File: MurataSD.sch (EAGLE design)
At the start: 2 parts, among them U1 IC_BLE_LBCA2HNZYZ-711, U100 BOARD_MMC

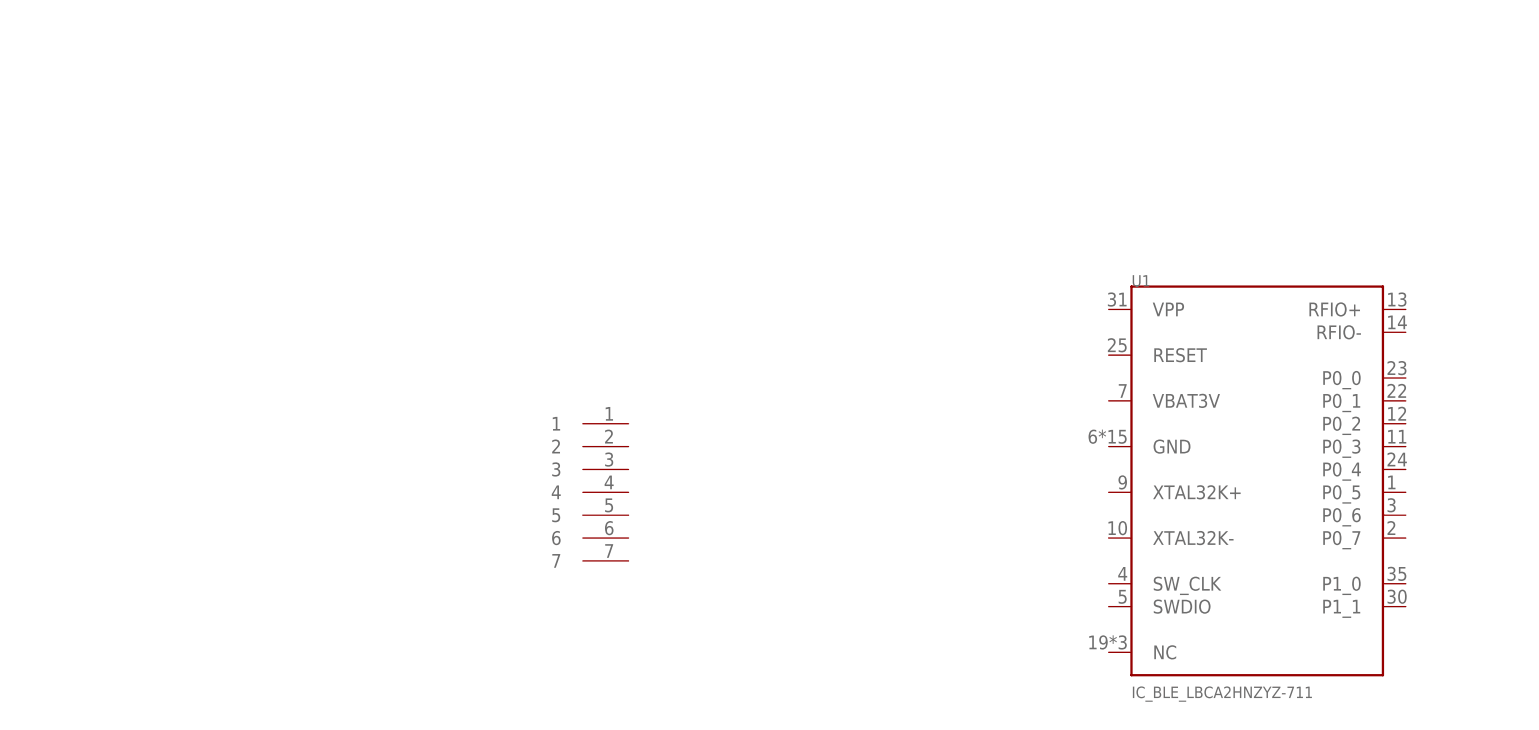
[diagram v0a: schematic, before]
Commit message: schematic update
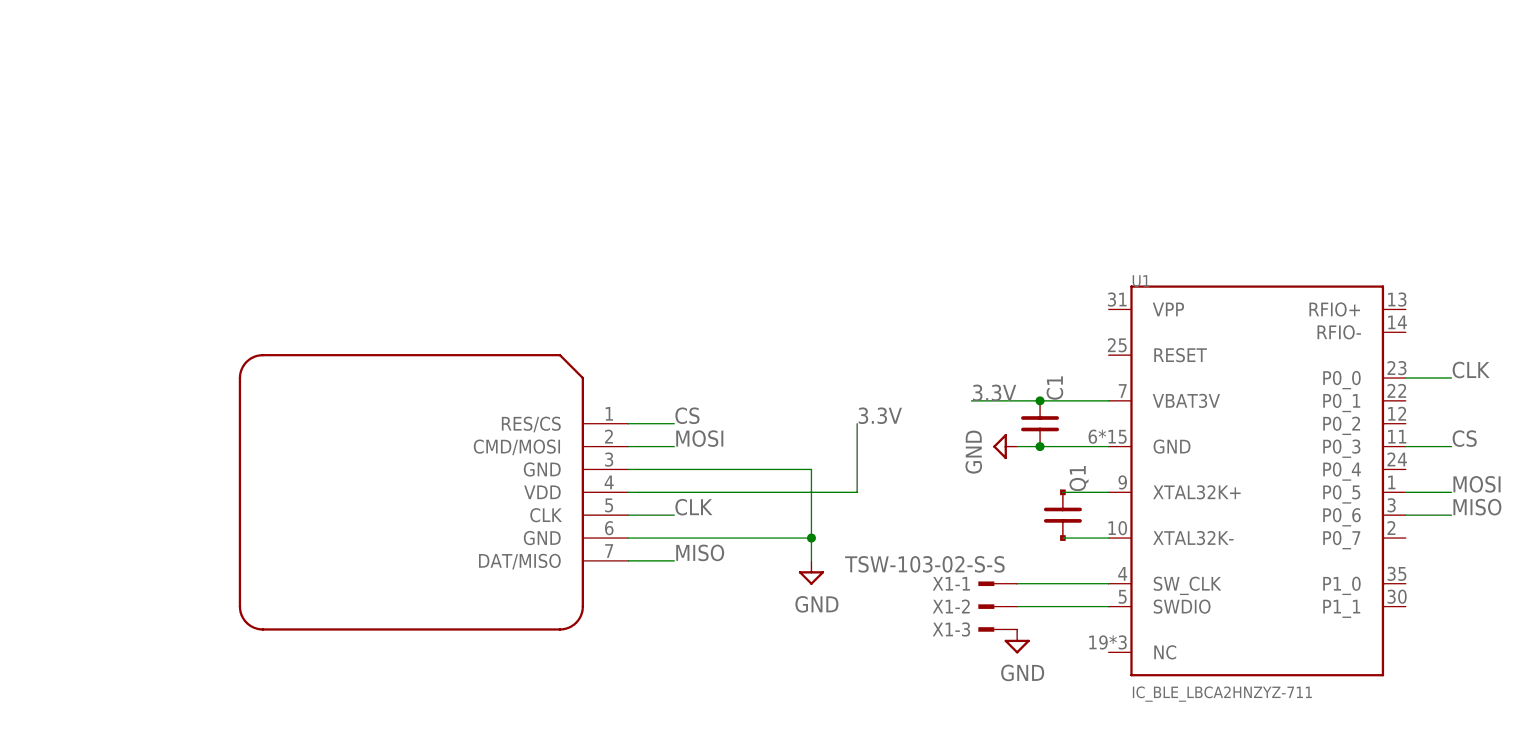
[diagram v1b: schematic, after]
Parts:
- added C1: (no value), mylib:C_PAD_PAD_1005
- added Q1: (no value), mylib:C_PAD_PAD_3216
- added X1: TSW-103-02-S-S, con-samtec.local:TSW-103-02-S-S
- renumbered U100 to U2
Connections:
- new net 3.3V: C1.1, U1.VBAT3V, U2.VDD
- new net CLK: U1.P0_0, U2.CLK
- new net CS: U1.P0_3, U2.RES/CS
- new net GND: C1.2, U1.GND, U2.GND@1, U2.GND@2, X1-3.1
- new net MISO: U1.P0_6, U2.DAT/MISO
- new net MOSI: U1.P0_5, U2.CMD/MOSI
- new net N$1: Q1.1, U1.XTAL32K+
- new net N$2: Q1.2, U1.XTAL32K-
- new net N$3: U1.SW_CLK, X1-1.1
- new net N$4: U1.SWDIO, X1-2.1
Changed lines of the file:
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@@
 <parts>
 <part name="FRAME1" library="frames" deviceset="A4L-LOC" device=""/>
-<part name="U100" library="mylib" deviceset="BOARD_MMC" device=""/>
+<part name="U2" library="mylib" deviceset="BOARD_MMC" device=""/>
 <part name="U1" library="mylib" deviceset="IC_BLE_LBCA2HNZYZ-711" device=""/>
+<part name="SUPPLY1" library="mylib" deviceset="GND" device=""/>
+<part name="SUPPLY2" library="mylib" deviceset="GND" device=""/>
+<part name="C1" library="mylib" deviceset="C_PAD_PAD_" device="1005"/>
+<part name="Q1" library="mylib" deviceset="C_PAD_PAD_" device="3216"/>
+<part name="X1" library="con-samtec.local" deviceset="TSW-103-02-S-S" device=""/>
+<part name="SUPPLY3" library="mylib" deviceset="GND" device=""/>
 </parts>
 <sheets>
@@
 <instances>
 <instance part="FRAME1" gate="G$1" x="0" y="0"/>
-<instance part="U100" gate="G$1" x="78.74" y="96.52"/>
+<instance part="U2" gate="G$1" x="78.74" y="96.52"/>
 <instance part="U1" gate="G$1" x="154.94" y="99.06"/>
+<instance part="SUPPLY1" gate="GND" x="124.46" y="101.6" rot="R270"/>
+<instance part="SUPPLY2" gate="GND" x="104.14" y="86.36"/>
+<instance part="C1" gate="G$1" x="129.54" y="104.14"/>
+<instance part="Q1" gate="G$1" x="132.08" y="93.98"/>
+<instance part="X1" gate="-1" x="124.46" y="86.36" rot="MR0"/>
+<instance part="X1" gate="-2" x="124.46" y="83.82" rot="MR0"/>
+<instance part="X1" gate="-3" x="124.46" y="81.28" rot="R180"/>
+<instance part="SUPPLY3" gate="GND" x="127" y="78.74"/>
 </instances>
 <busses>
 </busses>
 <nets>
+<net name="GND" class="0">
+<segment>
+<pinref part="U2" gate="G$1" pin="GND@1"/>
+<pinref part="SUPPLY2" gate="GND" pin="GND"/>
+<wire x1="83.82" y1="99.06" x2="104.14" y2="99.06" width="0.1524" layer="91"/>
+<wire x1="104.14" y1="99.06" x2="104.14" y2="91.44" width="0.1524" layer="91"/>
+<pinref part="U2" gate="G$1" pin="GND@2"/>
+<wire x1="104.14" y1="91.44" x2="104.14" y2="88.9" width="0.1524" layer="91"/>
+<wire x1="83.82" y1="91.44" x2="104.14" y2="91.44" width="0.1524" layer="91"/>
+<junction x="104.14" y="91.44"/>
+</segment>
+<segment>
+<pinref part="SUPPLY1" gate="GND" pin="GND"/>
+<pinref part="C1" gate="G$1" pin="2"/>
+<wire x1="127" y1="101.6" x2="129.54" y2="101.6" width="0.1524" layer="91"/>
+<pinref part="U1" gate="G$1" pin="GND"/>
+<wire x1="129.54" y1="101.6" x2="137.16" y2="101.6" width="0.1524" layer="91"/>
+<junction x="129.54" y="101.6"/>
+</segment>
+<segment>
+<pinref part="X1" gate="-3" pin="1"/>
+<pinref part="SUPPLY3" gate="GND" pin="GND"/>
+</segment>
+</net>
+<net name="3.3V" class="0">
+<segment>
+<pinref part="U2" gate="G$1" pin="VDD"/>
+<wire x1="83.82" y1="96.52" x2="109.22" y2="96.52" width="0.1524" layer="91"/>
+<wire x1="109.22" y1="96.52" x2="109.22" y2="104.14" width="0.1524" layer="91"/>
+<label x="109.22" y="104.14" size="1.778" layer="95"/>
+</segment>
+<segment>
+<pinref part="U1" gate="G$1" pin="VBAT3V"/>
+<pinref part="C1" gate="G$1" pin="1"/>
+<wire x1="137.16" y1="106.68" x2="129.54" y2="106.68" width="0.1524" layer="91"/>
+<wire x1="129.54" y1="106.68" x2="121.92" y2="106.68" width="0.1524" layer="91"/>
+<junction x="129.54" y="106.68"/>
+<label x="121.92" y="106.68" size="1.778" layer="95"/>
+</segment>
+</net>
+<net name="N$1" class="0">
+<segment>
+<pinref part="U1" gate="G$1" pin="XTAL32K+"/>
+<pinref part="Q1" gate="G$1" pin="1"/>
+<wire x1="137.16" y1="96.52" x2="132.08" y2="96.52" width="0.1524" layer="91"/>
+</segment>
+</net>
+<net name="N$2" class="0">
+<segment>
+<pinref part="U1" gate="G$1" pin="XTAL32K-"/>
+<pinref part="Q1" gate="G$1" pin="2"/>
+<wire x1="137.16" y1="91.44" x2="132.08" y2="91.44" width="0.1524" layer="91"/>
+</segment>
+</net>
+<net name="CLK" class="0">
+<segment>
+<pinref part="U2" gate="G$1" pin="CLK"/>
+<wire x1="83.82" y1="93.98" x2="88.9" y2="93.98" width="0.1524" layer="91"/>
+<label x="88.9" y="93.98" size="1.778" layer="95"/>
+</segment>
+<segment>
+<wire x1="170.18" y1="109.22" x2="175.26" y2="109.22" width="0.1524" layer="91"/>
+<pinref part="U1" gate="G$1" pin="P0_0"/>
+<label x="175.26" y="109.22" size="1.778" layer="95"/>
+</segment>
+</net>
+<net name="MOSI" class="0">
+<segment>
+<pinref part="U2" gate="G$1" pin="CMD/MOSI"/>
+<wire x1="83.82" y1="101.6" x2="88.9" y2="101.6" width="0.1524" layer="91"/>
+<label x="88.9" y="101.6" size="1.778" layer="95"/>
+</segment>
+<segment>
+<wire x1="170.18" y1="96.52" x2="175.26" y2="96.52" width="0.1524" layer="91"/>
+<pinref part="U1" gate="G$1" pin="P0_5"/>
+<label x="175.26" y="96.52" size="1.778" layer="95"/>
+</segment>
+</net>
+<net name="CS" class="0">
+<segment>
+<pinref part="U2" gate="G$1" pin="RES/CS"/>
+<wire x1="83.82" y1="104.14" x2="88.9" y2="104.14" width="0.1524" layer="91"/>
+<label x="88.9" y="104.14" size="1.778" layer="95"/>
+</segment>
+<segment>
+<wire x1="170.18" y1="101.6" x2="175.26" y2="101.6" width="0.1524" layer="91"/>
+<pinref part="U1" gate="G$1" pin="P0_3"/>
+<label x="175.26" y="101.6" size="1.778" layer="95"/>
+</segment>
+</net>
+<net name="MISO" class="0">
+<segment>
+<pinref part="U2" gate="G$1" pin="DAT/MISO"/>
+<wire x1="83.82" y1="88.9" x2="88.9" y2="88.9" width="0.1524" layer="91"/>
+<label x="88.9" y="88.9" size="1.778" layer="95"/>
+</segment>
+<segment>
+<wire x1="170.18" y1="93.98" x2="175.26" y2="93.98" width="0.1524" layer="91"/>
+<label x="175.26" y="93.98" size="1.778" layer="95"/>
+<pinref part="U1" gate="G$1" pin="P0_6"/>
+</segment>
+</net>
+<net name="N$3" class="0">
+<segment>
+<pinref part="U1" gate="G$1" pin="SW_CLK"/>
+<wire x1="127" y1="86.36" x2="137.16" y2="86.36" width="0.1524" layer="91"/>
+<pinref part="X1" gate="-1" pin="1"/>
+</segment>
+</net>
+<net name="N$4" class="0">
+<segment>
+<pinref part="U1" gate="G$1" pin="SWDIO"/>
+<wire x1="137.16" y1="83.82" x2="127" y2="83.82" width="0.1524" layer="91"/>
+<pinref part="X1" gate="-2" pin="1"/>
+</segment>
+</net>
 </nets>
 </sheet>

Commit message: [ SD ] update library
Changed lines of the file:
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@@
 <layers>
 <layer number="1" name="Top" color="4" fill="1" visible="no" active="no"/>
+<layer number="2" name="Route2" color="1" fill="3" visible="no" active="no"/>
+<layer number="3" name="Route3" color="4" fill="3" visible="no" active="no"/>
+<layer number="14" name="Route14" color="1" fill="6" visible="no" active="no"/>
+<layer number="15" name="Route15" color="4" fill="6" visible="no" active="no"/>
 <layer number="16" name="Bottom" color="1" fill="1" visible="no" active="no"/>
 <layer number="17" name="Pads" color="2" fill="1" visible="no" active="no"/>
@@
 <layer number="132" name="bAdjust" color="7" fill="1" visible="no" active="yes"/>
 <layer number="144" name="Drill_legend" color="7" fill="1" visible="yes" active="yes"/>
+<layer number="145" name="DrillLegend_01-16" color="2" fill="9" visible="no" active="yes"/>
+<layer number="146" name="DrillLegend_01-20" color="3" fill="9" visible="no" active="yes"/>
 <layer number="151" name="HeatSink" color="7" fill="1" visible="yes" active="yes"/>
 <layer number="152" name="_bDocu" color="7" fill="1" visible="yes" active="yes"/>

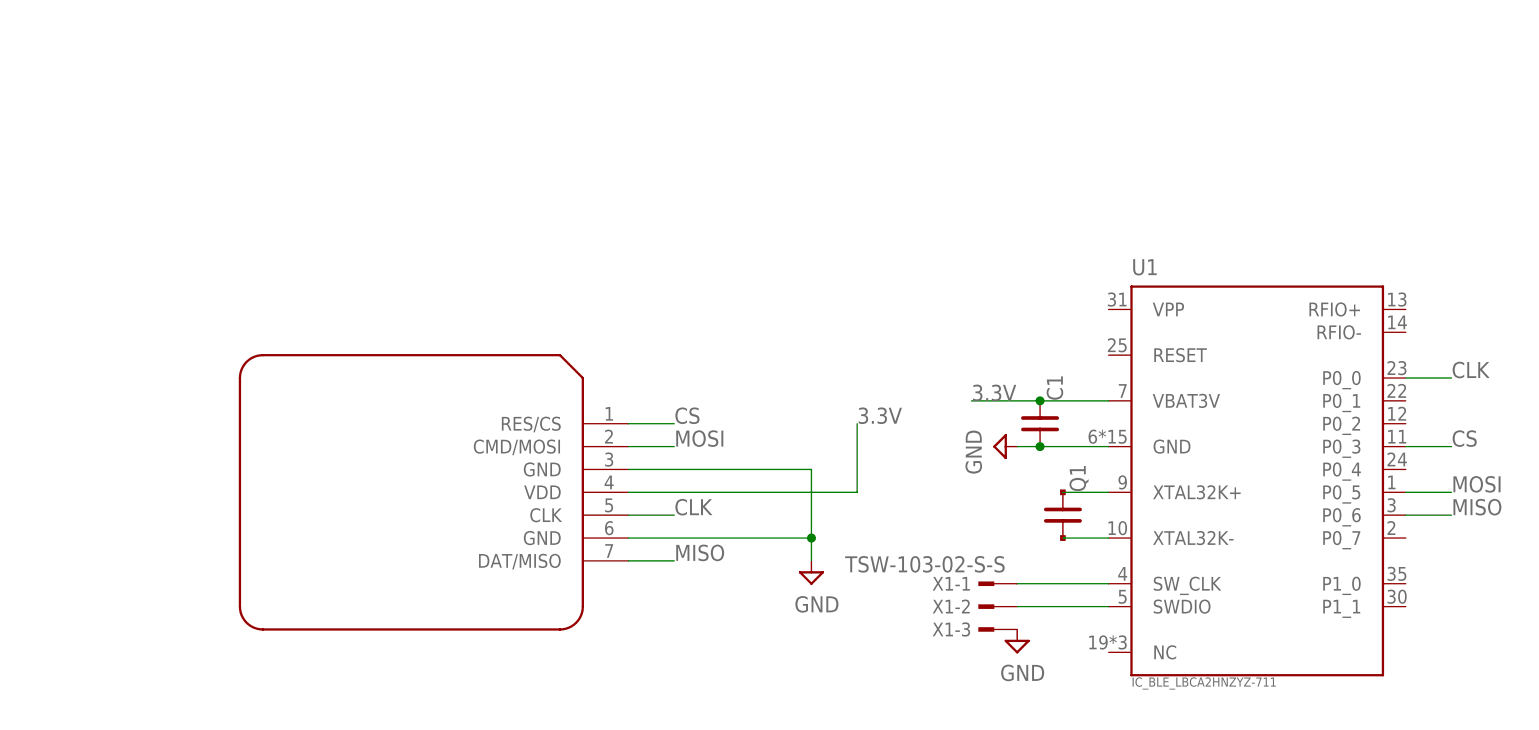
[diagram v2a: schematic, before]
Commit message: [ SD ] library update; add SWD connector; add Flash;
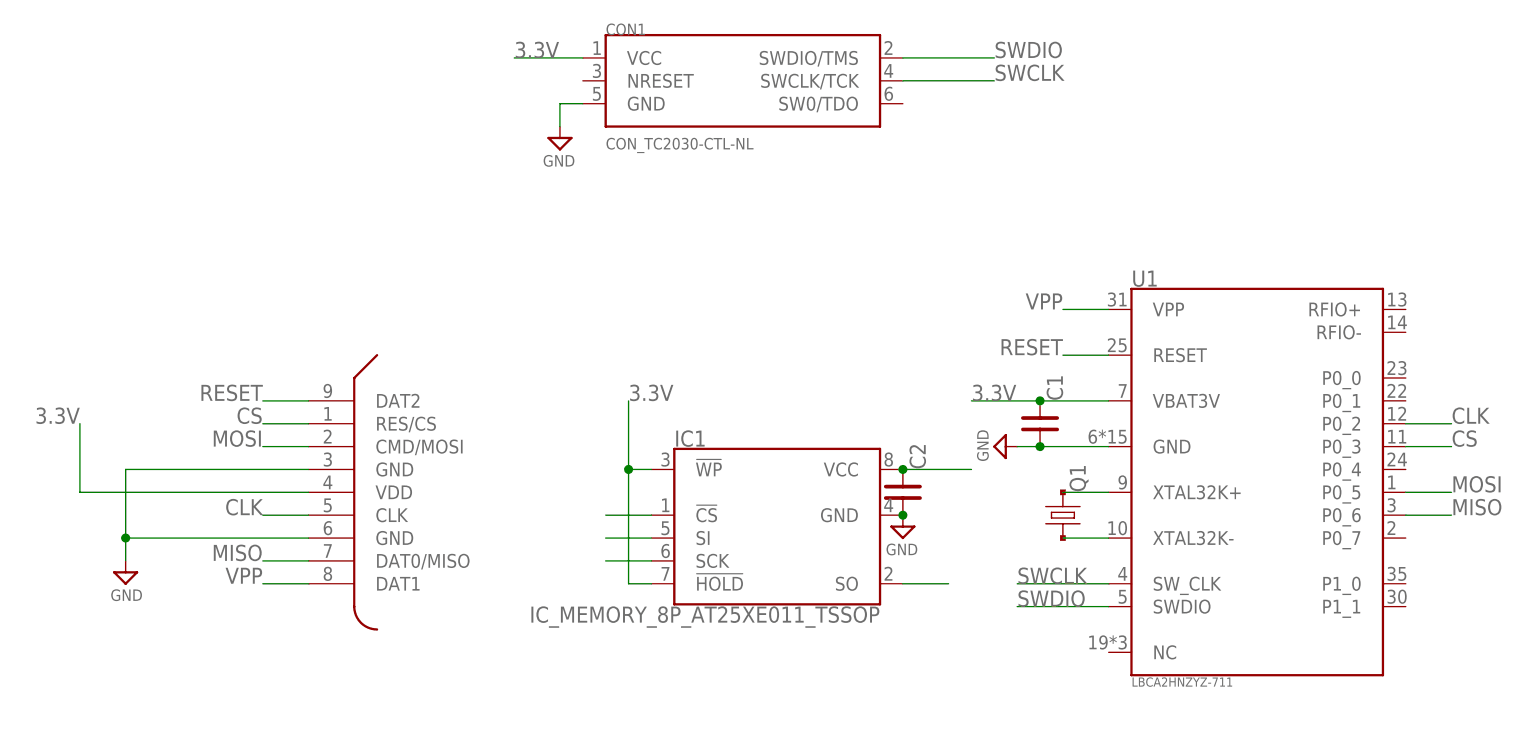
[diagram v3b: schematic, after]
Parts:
- removed X1: TSW-103-02-S-S, con-samtec.local:TSW-103-02-S-S
- added C2: (no value), mylib:C_SMD_0.1U_1005
- added CON1: CON_TC2030-CTL-NL, mylib:CON_TC2030-CTL-NL
- added IC1: IC_MEMORY_8P_AT25XE011_TSSOP, mylib:IC_MEMORY_8P_AT25XE011_TSSOP
- C1: device mylib:C_PAD_PAD_1005 -> mylib:C_SMD_0.1U_1005
- Q1: device mylib:C_PAD_PAD_3216 -> mylib:CRYSTAL2_32.768K_FC-135
- U1: value IC_BLE_LBCA2HNZYZ-711 -> LBCA2HNZYZ-711; device mylib:IC_BLE_LBCA2HNZYZ-711 -> mylib:LBCA2HNZYZ-711
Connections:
- removed net N$3: U1.SW_CLK, X1-1.1
- removed net N$4: U1.SWDIO, X1-2.1
- new net RESET: U1.RESET, U2.DAT2
- new net SWCLK: CON1.SWCLK/TCK, U1.SW_CLK
- new net SWDIO: CON1.SWDIO/TMS, U1.SWDIO
- new net VPP: U1.VPP, U2.DAT1
- net 3.3V: now also C2.1, CON1.VCC, IC1.!HOLD, IC1.!WP, IC1.VCC
- net CLK: now also IC1.SCK, U1.P0_2; no longer U1.P0_0
- net CS: now also IC1.!CS
- net GND: now also C2.2, CON1.GND, IC1.GND; no longer X1-3.1
- net MISO: now also IC1.SO, U2.DAT0/MISO; no longer U2.DAT/MISO
- net MOSI: now also IC1.SI

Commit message: [ SD ] disconnect VPP; SPI uses P0_4 to P0_7
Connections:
- removed net VPP: U1.VPP, U2.DAT1
- new net N$4: U1.P1_1, U2.DAT1
- new net N$5: U1.VPP
- net CLK: now also U1.P0_7; no longer U1.P0_2
- net CS: now also U1.P0_4; no longer U1.P0_3
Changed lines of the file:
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@@
 </segment>
 <segment>
-<wire x1="175.26" y1="104.14" x2="170.18" y2="104.14" width="0.1524" layer="91"/>
-<pinref part="U1" gate="G$1" pin="P0_2"/>
-<label x="175.26" y="104.14" size="1.778" layer="95"/>
+<wire x1="175.26" y1="91.44" x2="170.18" y2="91.44" width="0.1524" layer="91"/>
+<pinref part="U1" gate="G$1" pin="P0_7"/>
+<label x="175.26" y="91.44" size="1.778" layer="95"/>
 </segment>
 </net>
@@
 </segment>
 <segment>
-<wire x1="170.18" y1="101.6" x2="175.26" y2="101.6" width="0.1524" layer="91"/>
-<pinref part="U1" gate="G$1" pin="P0_3"/>
-<label x="175.26" y="101.6" size="1.778" layer="95"/>
+<wire x1="86.36" y1="93.98" x2="81.28" y2="93.98" width="0.1524" layer="91"/>
+<pinref part="IC1" gate="G$1" pin="!CS"/>
 </segment>
 <segment>
-<wire x1="86.36" y1="93.98" x2="81.28" y2="93.98" width="0.1524" layer="91"/>
-<pinref part="IC1" gate="G$1" pin="!CS"/>
+<wire x1="170.18" y1="99.06" x2="175.26" y2="99.06" width="0.1524" layer="91"/>
+<pinref part="U1" gate="G$1" pin="P0_4"/>
+<label x="175.26" y="99.06" size="1.778" layer="95"/>
 </segment>
 </net>
@@
 </segment>
 </net>
-<net name="VPP" class="0">
-<segment>
-<pinref part="U2" gate="G$1" pin="DAT1"/>
-<wire x1="48.26" y1="86.36" x2="43.18" y2="86.36" width="0.1524" layer="91"/>
-<label x="43.18" y="86.36" size="1.778" layer="95" rot="MR0"/>
-</segment>
-<segment>
-<wire x1="137.16" y1="116.84" x2="132.08" y2="116.84" width="0.1524" layer="91"/>
-<pinref part="U1" gate="G$1" pin="VPP"/>
-<label x="132.08" y="116.84" size="1.778" layer="95" rot="MR0"/>
-</segment>
-</net>
 <net name="RESET" class="0">
 <segment>
@@
 </segment>
 <segment>
-<wire x1="137.16" y1="111.76" x2="132.08" y2="111.76" width="0.1524" layer="91"/>
+<wire x1="137.16" y1="111.76" x2="134.62" y2="111.76" width="0.1524" layer="91"/>
 <pinref part="U1" gate="G$1" pin="RESET"/>
-<label x="132.08" y="111.76" size="1.778" layer="95" rot="MR0"/>
+<label x="121.92" y="114.3" size="1.778" layer="95" rot="MR0"/>
+<wire x1="134.62" y1="111.76" x2="134.62" y2="114.3" width="0.1524" layer="91"/>
+<wire x1="134.62" y1="114.3" x2="121.92" y2="114.3" width="0.1524" layer="91"/>
 </segment>
 </net>
+<net name="N$4" class="0">
+<segment>
+<pinref part="U2" gate="G$1" pin="DAT1"/>
+<wire x1="48.26" y1="86.36" x2="43.18" y2="86.36" width="0.1524" layer="91"/>
+<label x="43.18" y="86.36" size="1.778" layer="95" rot="MR0"/>
+</segment>
+<segment>
+<wire x1="175.26" y1="83.82" x2="170.18" y2="83.82" width="0.1524" layer="91"/>
+<pinref part="U1" gate="G$1" pin="P1_1"/>
+<label x="175.26" y="83.82" size="1.778" layer="95"/>
+</segment>
+</net>
+<net name="N$5" class="0">
+<segment>
+<pinref part="U1" gate="G$1" pin="VPP"/>
+<wire x1="137.16" y1="116.84" x2="134.62" y2="116.84" width="0.1524" layer="91"/>
+<junction x="134.62" y="116.84"/>
+</segment>
+</net>

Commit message: [ SD ]
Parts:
- Q1: value (none) -> CRYSTAL2_32.768K_2012; device mylib:CRYSTAL2_32.768K_FC-135 -> mylib:CRYSTAL2_32.768K_2012
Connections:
- net N$4: no longer U1.P1_1
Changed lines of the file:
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@@
 <part name="SUPPLY2" library="mylib" deviceset="GND" device=""/>
 <part name="C1" library="mylib" deviceset="C_SMD_*" device="_1005" technology="0.1U"/>
-<part name="Q1" library="mylib" deviceset="CRYSTAL2_*" device="_FC-135" technology="32.768K"/>
+<part name="Q1" library="mylib" deviceset="CRYSTAL2_*" device="_2012" technology="32.768K" value="CRYSTAL2_32.768K_2012"/>
 <part name="CON1" library="mylib" deviceset="CON_TC2030" device="-CTL-NL"/>
 <part name="IC1" library="mylib" deviceset="IC_MEMORY_8P_*" device="_TSSOP" technology="AT25XE011"/>
@@
 <label x="43.18" y="86.36" size="1.778" layer="95" rot="MR0"/>
 </segment>
-<segment>
-<wire x1="175.26" y1="83.82" x2="170.18" y2="83.82" width="0.1524" layer="91"/>
-<pinref part="U1" gate="G$1" pin="P1_1"/>
-<label x="175.26" y="83.82" size="1.778" layer="95"/>
-</segment>
-</net>
+</net>
